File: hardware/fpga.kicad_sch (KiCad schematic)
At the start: 14 parts, among them U15 SN74ALVC164245, U16 SN74ALVC164245, U17 SN74ALVC164245, U18 SN74ALVC164245, U2 ICE40HX4K-TQ144, U5 W25Q32JVSSIM, U8 LTC6905xS5-133

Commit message: updates
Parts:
- added U26: iCE40HX8K-CT256(256-Ball_caBGA), 68040:256-Ball_caBGA(Pitch_0.80mm_Pad_0.40mm), symbol 68040:iCE40HX8K-CT256(256-Ball_caBGA)
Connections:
- net +3.3V: now also U26.J6 (VCCIO_3)
- net DRAM_A0: now also U2.52 (IOB_82_GBIN4); no longer U2.37 (IOB_56)
- net DRAM_A1: now also U2.49 (IOB_81_GBIN5); no longer U2.38 (IOB_57)
- net DRAM_A10: now also U2.42 (IOB_64); no longer U2.45 (IOB_73)
- net DRAM_A11: now also U2.39 (IOB_61); no longer U2.48 (IOB_80)
- net DRAM_A2: now also U2.48 (IOB_80); no longer U2.39 (IOB_61)
- net DRAM_A3: now also U2.47 (IOB_79); no longer U2.41 (IOB_63)
- net DRAM_A4: now also U2.45 (IOB_73); no longer U2.42 (IOB_64)
- net DRAM_A5: now also U2.44 (IOB_72); no longer U2.43 (IOB_71)
- net DRAM_A6: now also U2.43 (IOB_71); no longer U2.44 (IOB_72)
- net DRAM_A7: now also U2.41 (IOB_63); no longer U2.47 (IOB_79)
- net DRAM_A8: now also U2.38 (IOB_57); no longer U2.49 (IOB_81_GBIN5)
- net DRAM_A9: now also U2.37 (IOB_56); no longer U2.52 (IOB_82_GBIN4)
- net GND: now also U26.A12 (GND), U26.A4 (GND), U26.E15 (GND), U26.E7 (GNDPLL1), U26.G7 (GND), U26.G8 (GND), U26.G9 (GND), U26.H7 (GND), U26.H8 (GND), U26.H9 (GND), U26.J7 (GND), U26.J8 (GND), U26.J9 (GND), U26.K2 (GND), U26.K7 (GND), U26.L15 (GND), U26.N8 (GNDPLL0), U26.R7 (GND), U26.T12 (GND), U26.T4 (GND)

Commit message: update cpu symbol, topology
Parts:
- removed RN5: 10k, Resistor_THT:R_Array_SIP5, symbol Device:R_Network04_US
- removed unit 2 of U15
- removed unit 2 of U16
- removed U26: iCE40HX8K-CT256(256-Ball_caBGA), 68040:256-Ball_caBGA(Pitch_0.80mm_Pad_0.40mm), symbol 68040:iCE40HX8K-CT256(256-Ball_caBGA)
- added D2: D_Schottky, symbol Device:D_Schottky
- added J5: Conn_01x06, symbol Connector_Generic:Conn_01x06
- added U17, U18: SN74ALVC164245, Package_SO:TSSOP-48_6.1x12.5mm_P0.5mm, symbol 68040:SN74ALVC164245
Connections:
- net ~{RAS1} is gone; now on net FLASH_IO2: U2.61 (IOB_96)
- net +3V3: now also U2.72 (VCC_SPI), D2.2 (A), U17.31 (VCCA), U17.42 (VCCA), U18.31 (VCCA), U18.42 (VCCA); no longer C17.1, R8.2, R9.2, U5.8 (VCC)
- net +5V: now also U17.18 (VCCB), U17.7 (VCCB), U18.18 (VCCB), U18.7 (VCCB)
- net FLASH_MISO: now also J5.5 (Pin_5)
- net FLASH_MOSI: now also J5.4 (Pin_4)
- net FLASH_SCK: now also J5.6 (Pin_6)
- net FLASH_SS: now also J5.1 (Pin_1)
- net GND: now also J5.3 (Pin_3), U17.10 (GND), U17.15 (GND), U17.21 (GND), U17.28 (GND), U17.34 (GND), U17.39 (GND), U17.4 (GND), U17.45 (GND), U18.10 (GND), U18.15 (GND), U18.21 (GND), U18.28 (GND), U18.34 (GND), U18.39 (GND), U18.4 (GND), U18.45 (GND)
- net FPGA_A_DIR: now reaches U15.1 (1DIR)
- net FPGA_A_DIR: now also U15.24 (2DIR), U16.1 (1DIR), U16.24 (2DIR)
- net ~{FPGA_A_OE}: now reaches U15.25 (*2OE)
- net ~{FPGA_A_OE}: now also U15.48 (*1OE), U16.25 (*2OE), U16.48 (*1OE)
- net FPGA_D_DIR: now reaches U18.1 (1DIR)
- net FPGA_D_DIR: now also U17.1 (1DIR), U17.24 (2DIR), U18.24 (2DIR)
- net ~{FPGA_D_OE}: now reaches U18.25 (*2OE)
- net ~{FPGA_D_OE}: now also U17.25 (*2OE), U17.48 (*1OE), U18.48 (*1OE)
- net FLASH_IO3: now reaches U2.62 (IOB_102)
- net FLASH_IO3: now also U5.7 (IO3)
- net FLASH_IO2: now reaches U5.3 (IO2)
- net DRAM_A0: no longer names the net of U2.52 (IOB_82_GBIN4)
- net DRAM_A1: no longer names the net of U2.49 (IOB_81_GBIN5)
- net DRAM_A10: no longer names the net of U2.42 (IOB_64)
- net DRAM_A11: no longer names the net of U2.39 (IOB_61)
- net DRAM_A2: no longer names the net of U2.48 (IOB_80)
- net DRAM_A3: no longer names the net of U2.47 (IOB_79)
- net DRAM_A4: no longer names the net of U2.45 (IOB_73)
- net DRAM_A5: no longer names the net of U2.44 (IOB_72)
- net DRAM_A6: no longer names the net of U2.43 (IOB_71)
- net DRAM_A7: no longer names the net of U2.41 (IOB_63)
- net DRAM_A8: no longer names the net of U2.38 (IOB_57)
- net DRAM_A9: no longer names the net of U2.37 (IOB_56)
- net PD_{A}1: no longer names the net of U2.11 (IOL_8A)
- net PD_{A}2: no longer names the net of U2.12 (IOL_8B)
- net PD_{A}3: no longer names the net of U2.15 (IOL_10A)
- net PD_{A}4: no longer names the net of U2.16 (IOL_10B)
- net ~{CAS_A0}: no longer names the net of U2.32 (IOL_24B)
- net ~{CAS_A1}: no longer names the net of U2.28 (IOL_23A)
- net ~{CAS_A2}: no longer names the net of U2.31 (IOL_24A)
- net ~{CAS_A3}: no longer names the net of U2.29 (IOL_23B)
- net ~{RAS0}: no longer names the net of U2.60 (IOB_95)
- net ~{RAS2}: no longer names the net of U2.56 (IOB_94)
- net ~{RAS3}: no longer names the net of U2.55 (IOB_91)
- new net FLASH_POWER: C17.1, D2.1 (K), J5.2 (Pin_2), R8.2, R9.2, U5.8 (VCC)
- no-connect marks 2 -> 0
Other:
- moved on the sheet: C17, D1, R7, R8, R9, U15A, U16A, U17A, U17B, U18A, U18B, U2E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

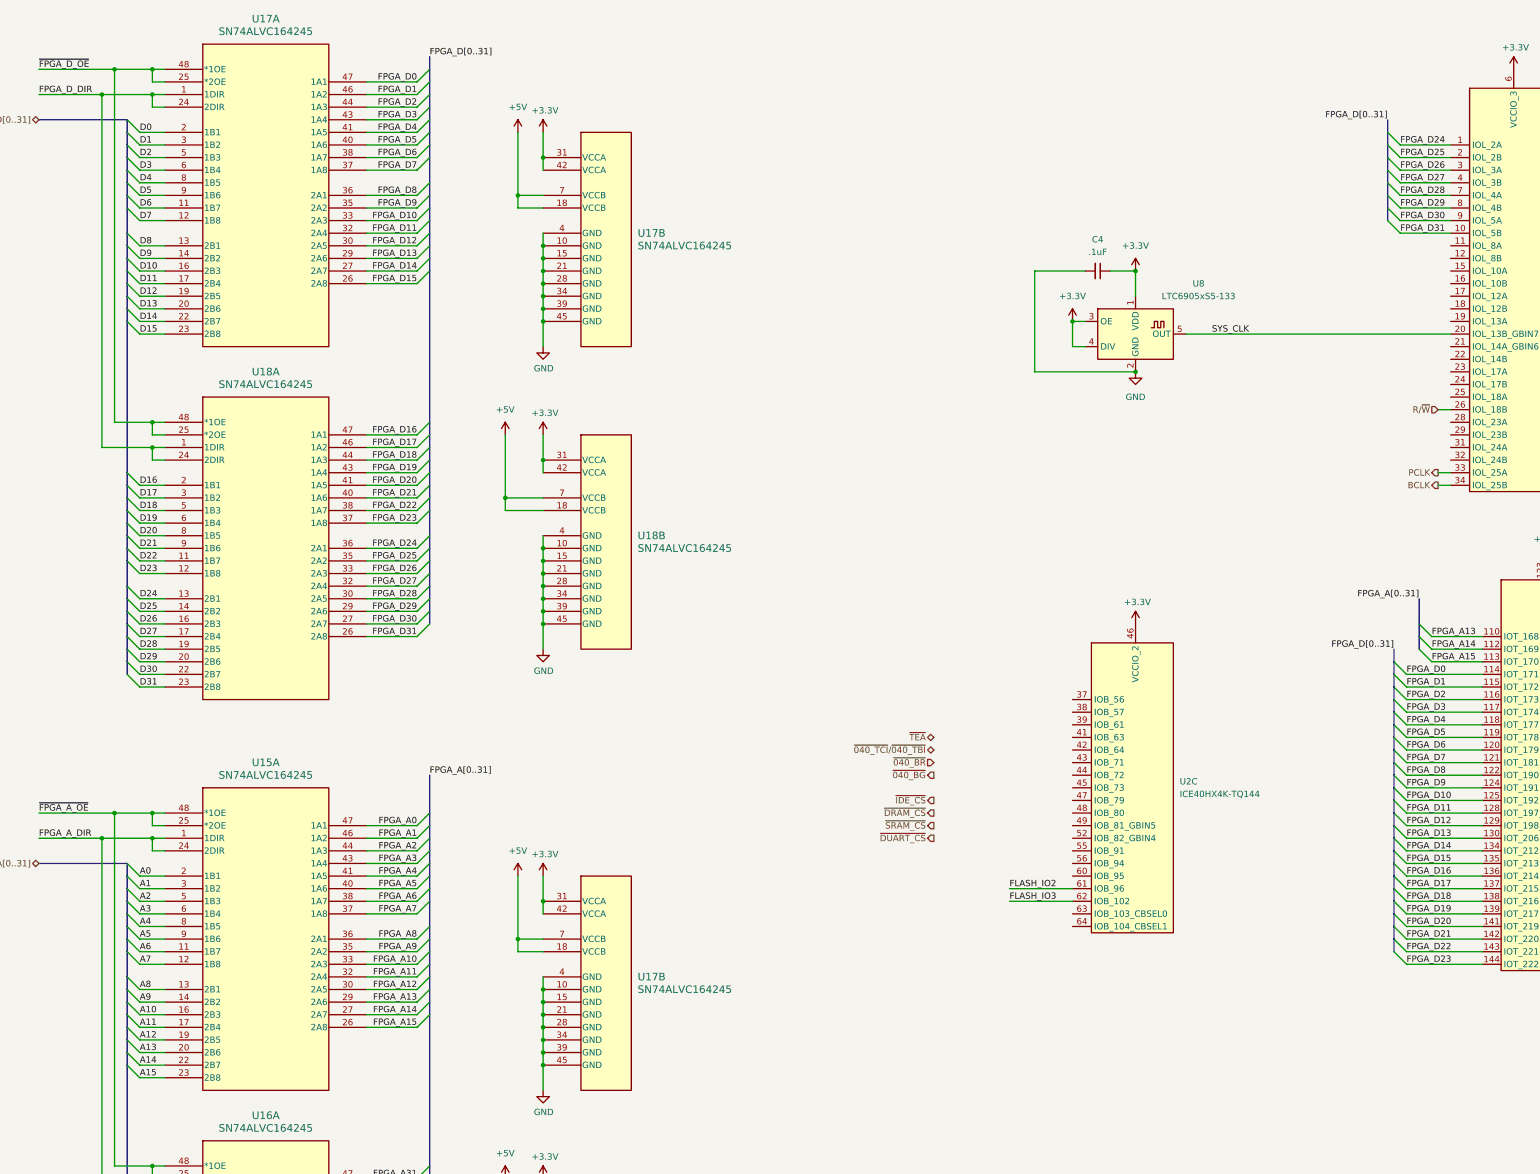
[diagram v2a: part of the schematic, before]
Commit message: add interrupt logic, clean up modules
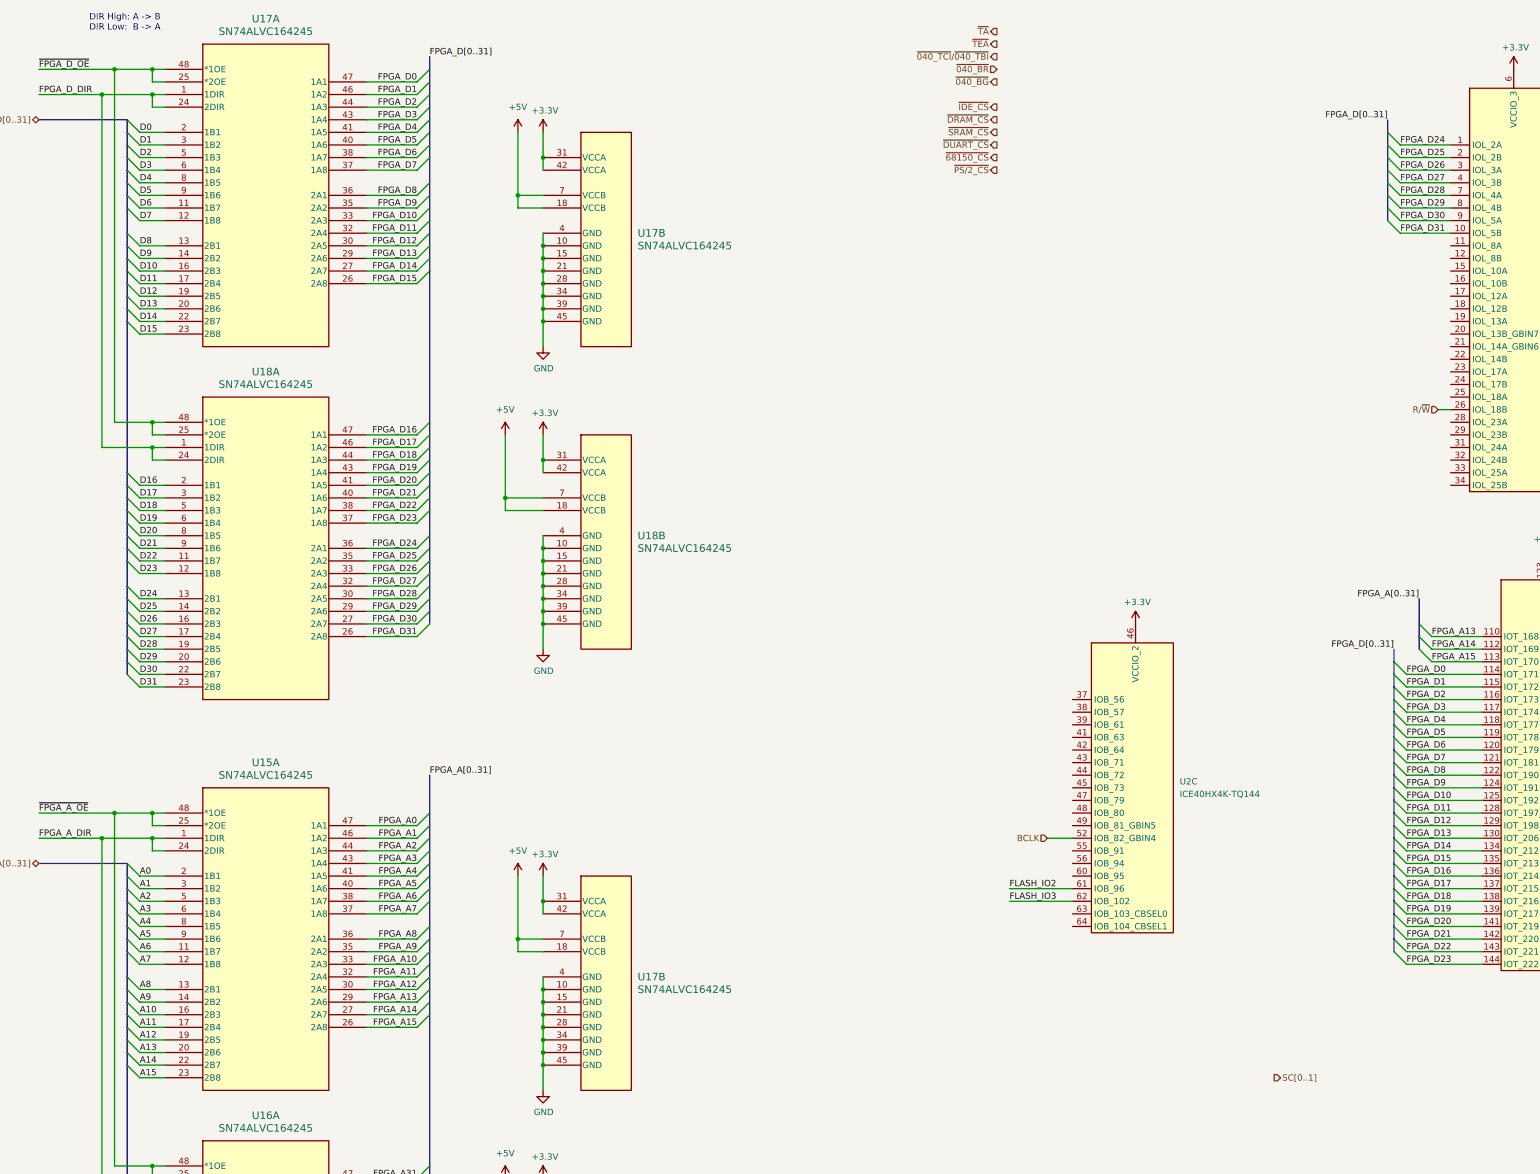
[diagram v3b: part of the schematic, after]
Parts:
- removed C4: .1uF, Capacitor_SMD:C_0603_1608Metric, symbol Device:C_Small
- removed U8: LTC6905xS5-133, Package_TO_SOT_SMD:TSOT-23-5, symbol Oscillator:LTC6905xS5-133
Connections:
- net BCLK: now also U2.52 (IOB_82_GBIN4); no longer U2.34 (IOL_25B)
- net PCLK: no longer names the net of U2.33 (IOL_25A)
- net SYS_CLK: no longer names the net of U2.20 (IOL_13B_GBIN7)
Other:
- note added: "DIR High: A -> B DIR Low: B -> A"

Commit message: updates
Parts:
- removed U15, U16, U17, U18: SN74ALVC164245, Package_SO:TSSOP-48_6.1x12.5mm_P0.5mm, symbol 68040:SN74ALVC164245

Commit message: getting closer
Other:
- moved on the sheet: C17, D1, D2, J5, R7, R8, R9, U2A, U2B, U2C, U2D, U2E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

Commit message: re-design level shifters
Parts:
- removed unit 2 of U17
- removed unit 1 of U18
- added C59, C60: .1uF, symbol Device:C_Small
- added R24: 4.7k, symbol Device:R_Small_US
- added RN2: 4.7k, Resistor_THT:R_Array_SIP5, symbol Device:R_Network04_US
- added U34, U35: 74AHCT04, symbol 74xx:74AHCT04
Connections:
- net +3V3: no longer U18.31 (VCCA), U18.42 (VCCA), U2.46 (VCCIO_2), U2.57 (VCCIO_2)
- net +5V: now also C59.1, C60.1, U34.14 (VCC), U35.14 (VCC)
- net FPGA_D_DIR: now also U2.64 (IOB_104_CBSEL1); no longer U17.24 (2DIR)
- net GND: now also U17.24 (2DIR), U17.25 (*2OE), C59.2, C60.2, U34.7 (GND), U35.7 (GND)
- net R/~{W}: no longer U2.26 (IOL_18B)
- net ~{040_BG}: now also U2.18 (IOL_12B)
- net ~{040_TCI}/~{040_TBI}: now also U2.17 (IOL_12A)
- net ~{68150_CS}: now also U34.10
- net ~{AVEC}: now also U35.2
- net ~{DRAM_CS}: now also U34.4
- net ~{DUART_CS}: now also U34.8
- net ~{FPGA_D_OE}: now also U2.25 (IOL_18A), R24.2; no longer U17.25 (*2OE)
- net ~{IDE_CS}: now also U34.2
- net ~{PS/2_CS}: now also U34.12
- net ~{SRAM_CS}: now also U34.6
- net ~{TA}: now also U2.15 (IOL_10A)
- net ~{TEA}: now also U2.16 (IOL_10B)
- net ~{CFG_{OUT}}: now reaches U2.11 (IOL_8A)
- net LV_~{CFG_{IN}}: now reaches U2.12 (IOL_8B)
- net LV_~{CFG_{IN}}: now also U17.33 (2A3)
- net LV_~{040_BR}: now reaches U2.19 (IOL_13A)
- net LV_~{LOCKE}: now reaches U2.20 (IOL_13B_GBIN7)
- net LV_~{LOCK}: now reaches U2.21 (IOL_14A_GBIN6)
- net LV_R/~{W}: now reaches U2.22 (IOL_14B)
- net LV_R/~{W}: now also U2.26 (IOL_18B)
- net LV_~{TS}: now reaches U2.23 (IOL_17A)
- net LV_~{68150_DS}: now reaches U2.24 (IOL_17B)
- net LV_IDE_CS: now reaches U2.28 (IOL_23A)
- net LV_IDE_CS: now also U34.1
- net LV_DRAM_CS: now reaches U2.29 (IOL_23B)
- net LV_DRAM_CS: now also U34.3
- net LV_SRAM_CS: now reaches U2.31 (IOL_24A)
- net LV_SRAM_CS: now also U34.5
- net LV_DUART_CS: now reaches U2.32 (IOL_24B)
- net LV_DUART_CS: now also U34.9
- net LV_68150_CS: now reaches U2.33 (IOL_25A)
- net LV_68150_CS: now also U34.11
- net LV_PS/2_CS: now reaches U2.34 (IOL_25B)
- net LV_PS/2_CS: now also U34.13
- net LV_AVEC: now reaches U2.63 (IOB_103_CBSEL0)
- net LV_AVEC: now also U35.1
- net D0 renamed PD24
- net D1 renamed PD25
- net D10 renamed ~{CFG_{IN}}
- net D11: no longer names the net of U17.17 (2B4)
- net D12: no longer names the net of U17.19 (2B5)
- net D13: no longer names the net of U17.20 (2B6)
- net D14: no longer names the net of U17.22 (2B7)
- net D15: no longer names the net of U17.23 (2B8)
- net D2 renamed PD26
- net D3 renamed PD27
- net D4 renamed PD28
- net D5 renamed PD29
- net D6 renamed PD30
- net D7 renamed PD31
- net D8 renamed PA0
- net D9 renamed PA1
- net FPGA_A0 renamed LV.A0
- net FPGA_A1 renamed LV.A1
- net FPGA_A10 renamed LV.A10
- net FPGA_A11 renamed LV.A11
- net FPGA_A12 renamed LV.A12
- net FPGA_A13 renamed LV.A13
- net FPGA_A14 renamed LV.A14
- net FPGA_A15 renamed LV.A15
- net FPGA_A16 renamed LV.A16
- net FPGA_A17 renamed LV.A17
- net FPGA_A18 renamed LV.A18
- net FPGA_A19 renamed LV.A19
- net FPGA_A2 renamed LV.A2
- net FPGA_A20 renamed LV.A20
- net FPGA_A21 renamed LV.A21
- net FPGA_A22 renamed LV.A22
- net FPGA_A23 renamed LV.A23
- net FPGA_A24 renamed LV.A24
- net FPGA_A25 renamed LV.A25
- net FPGA_A26 renamed LV.A26
- net FPGA_A27 renamed LV.A27
- net FPGA_A28 renamed LV.A28
- net FPGA_A29 renamed LV.A29
- net FPGA_A3 renamed LV.A3
- net FPGA_A30 renamed LV.A30
- net FPGA_A31 renamed LV.A31
- net FPGA_A4 renamed LV.A4
- net FPGA_A5 renamed LV.A5
- net FPGA_A6 renamed LV.A6
- net FPGA_A7 renamed LV.A7
- net FPGA_A8 renamed LV.A8
- net FPGA_A9 renamed LV.A9
- net FPGA_D10: no longer names the net of U2.125 (IOT_192)
- net FPGA_D10: no longer U17.33 (2A3)
- net FPGA_D11: no longer names the net of U2.128 (IOT_197_GBIN1)
- net FPGA_D11: no longer U17.32 (2A4)
- net FPGA_D12: no longer names the net of U2.129 (IOT_198_GBIN0)
- net FPGA_D12: no longer U17.30 (2A5)
- net FPGA_D13: no longer names the net of U2.130 (IOT_206)
- net FPGA_D13: no longer U17.29 (2A6)
- net FPGA_D14: no longer names the net of U2.134 (IOT_212)
- net FPGA_D14: no longer U17.27 (2A7)
- net FPGA_D15: no longer names the net of U2.135 (IOT_213)
- net FPGA_D15: no longer U17.26 (2A8)
- net FPGA_D16: no longer names the net of U2.136 (IOT_214)
- net FPGA_D17: no longer names the net of U2.137 (IOT_215)
- net FPGA_D18: no longer names the net of U2.138 (IOT_216)
- net FPGA_D19: no longer names the net of U2.139 (IOT_217)
- net FPGA_D20: no longer names the net of U2.141 (IOT_219)
- net FPGA_D21: no longer names the net of U2.142 (IOT_220)
- net FPGA_D22: no longer names the net of U2.143 (IOT_221)
- net FPGA_D23: no longer names the net of U2.144 (IOT_222)
- net FPGA_D24 renamed ~{DSACK0}
- net FPGA_D25 renamed ~{DSACK1}
- net FPGA_D26 renamed SC0
- net FPGA_D27 renamed SC1
- net FPGA_D28 renamed EXD_DIR
- net EXD_DIR: now also RN2.2 (R1)
- net FPGA_D29 renamed ~{EXD_OE}
- net ~{EXD_OE}: now also RN2.3 (R2)
- net FPGA_D30 renamed EXA_DIR
- net EXA_DIR: now also RN2.4 (R3)
- net FPGA_D31 renamed ~{EXA_OE}
- net ~{EXA_OE}: now also RN2.5 (R4)
- net FPGA_D8 renamed LV_PA0
- net FPGA_D9 renamed LV_PA1
- new net: U2.46 (VCCIO_2), U2.57 (VCCIO_2)
- new net +3.3V: R24.1, RN2.1 (common), U18.31 (VCCA), U18.42 (VCCA)
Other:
- added sheet AddressBuffer (fpga_abuf.kicad_sch)
- added sheet TransferBuffer (fpga_tbuf.kicad_sch)
- note added: "Bias to output disabled, board -> exp"
- moved on the sheet: U18B, U2A, U2B, U2C, U2D
